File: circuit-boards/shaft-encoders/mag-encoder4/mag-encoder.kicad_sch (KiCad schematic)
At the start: 25 parts, among them J1 CONFIG, J2 0015912055, U1 AP2120N-3.3TRG1, U2 SN74LVC7032ABQAR, U3 MA732GQ

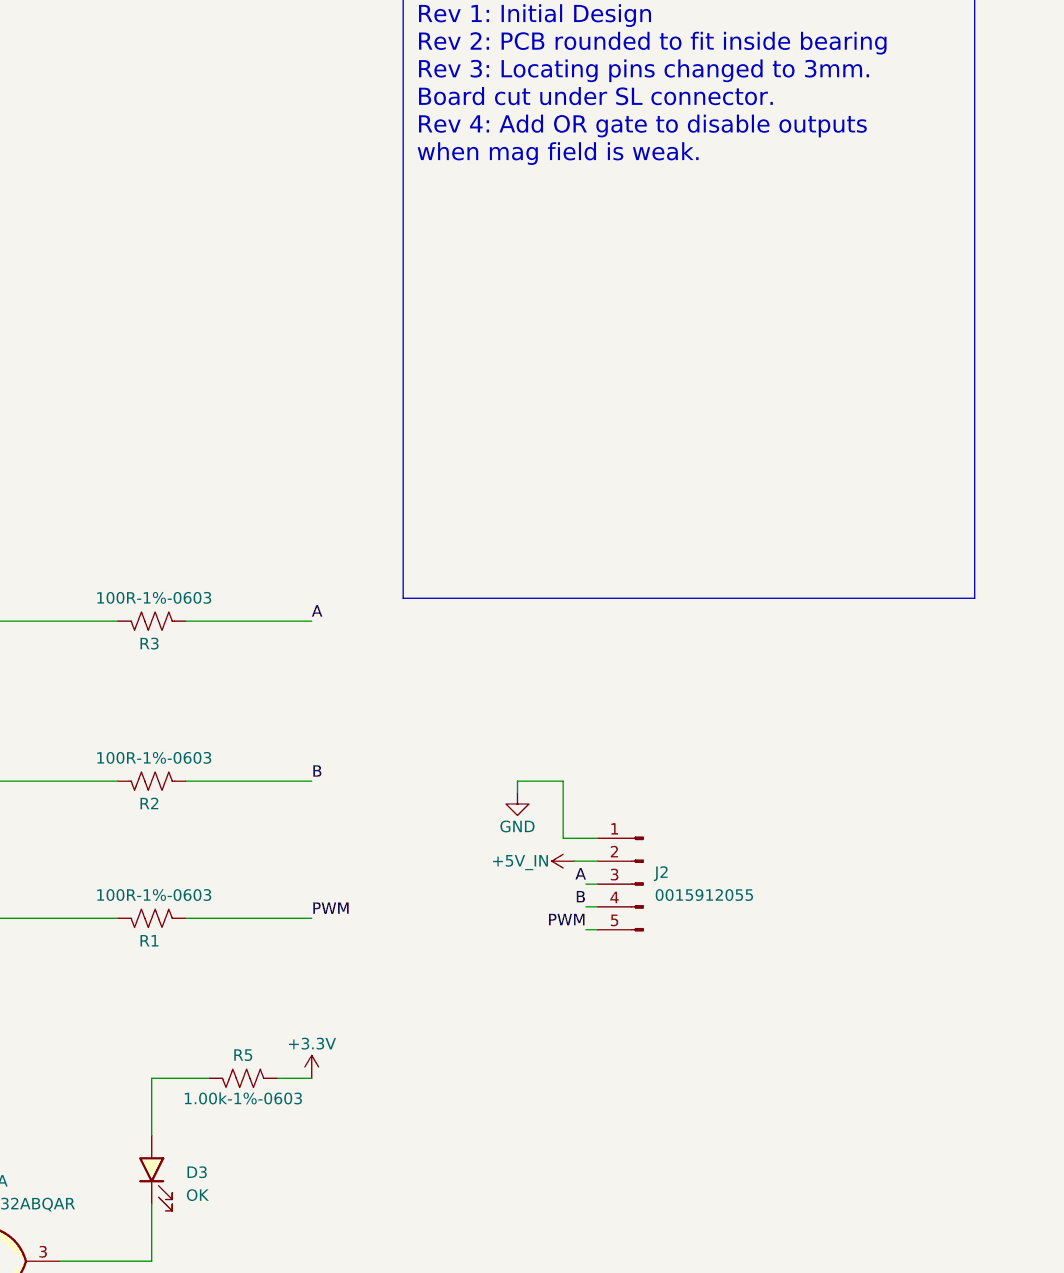
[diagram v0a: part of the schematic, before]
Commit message: Change Green LED current to 5mA
Signed-off-by: scott <sgberman1@gmail.com>
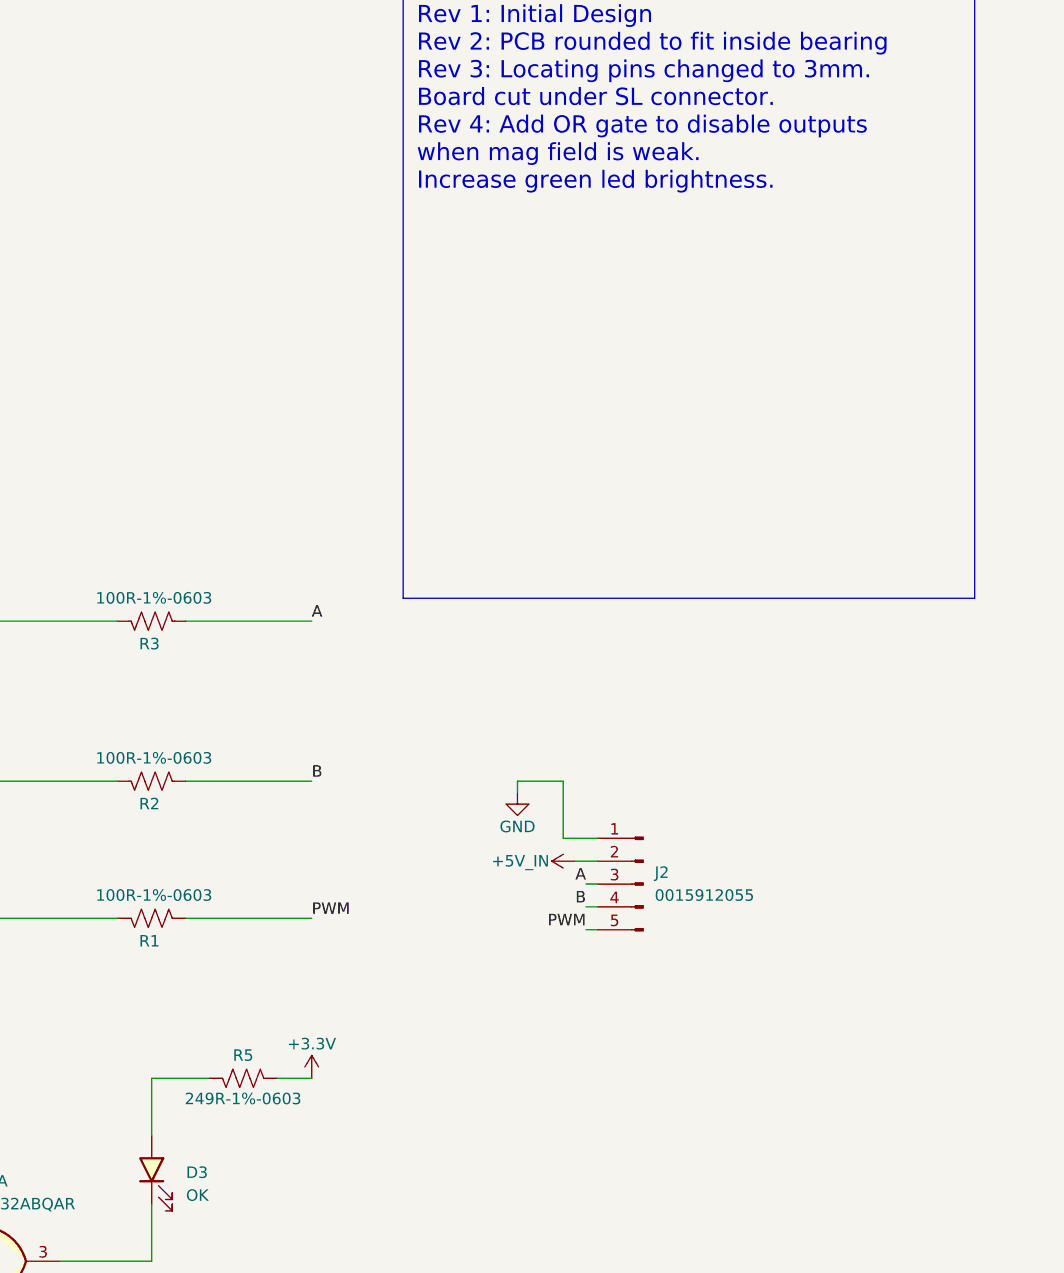
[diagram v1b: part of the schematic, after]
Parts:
- R5: value 1.00k-1%-0603 -> 249R-1%-0603; DIST P/N 311-1.00KHRCT-ND -> 311-249HRCT-ND; MFG P/N RC0603FR-071KL -> RC0603FR-07249RL
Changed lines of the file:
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@@
 	(title_block
 		(title "Mag Encoder")
-		(date "2024-11-25")
+		(date "2024-12-03")
 		(rev "4")
 		(company "971 SPARTAN ROBOTICS")
@@
 		)
 	)
-	(text_box "REVISION NOTES\n=======================\nRev 1: Initial Design\nRev 2: PCB rounded to fit inside bearing\nRev 3: Locating pins changed to 3mm.\n       Board cut under SL connector.\nRev 4: Add OR gate to disable outputs\n       when mag field is weak."
+	(text_box "REVISION NOTES\n=======================\nRev 1: Initial Design\nRev 2: PCB rounded to fit inside bearing\nRev 3: Locating pins changed to 3mm.\n       Board cut under SL connector.\nRev 4: Add OR gate to disable outputs\n       when mag field is weak.\n       Increase green led brightness."
 		(exclude_from_sim no)
 		(at 350.52 17.78 0)
@@
 			)
 		)
-		(property "Value" "1.00k-1%-0603"
+		(property "Value" "249R-1%-0603"
 			(at 332.74 147.066 90)
 			(effects
@@
 			)
 		)
-		(property "DIST P/N" "311-1.00KHRCT-ND"
+		(property "DIST P/N" "311-249HRCT-ND"
 			(at 332.74 144.78 0)
 			(effects
@@
 			)
 		)
-		(property "MFG P/N" "RC0603FR-071KL"
+		(property "MFG P/N" "RC0603FR-07249RL"
 			(at 332.74 144.78 0)
 			(effects

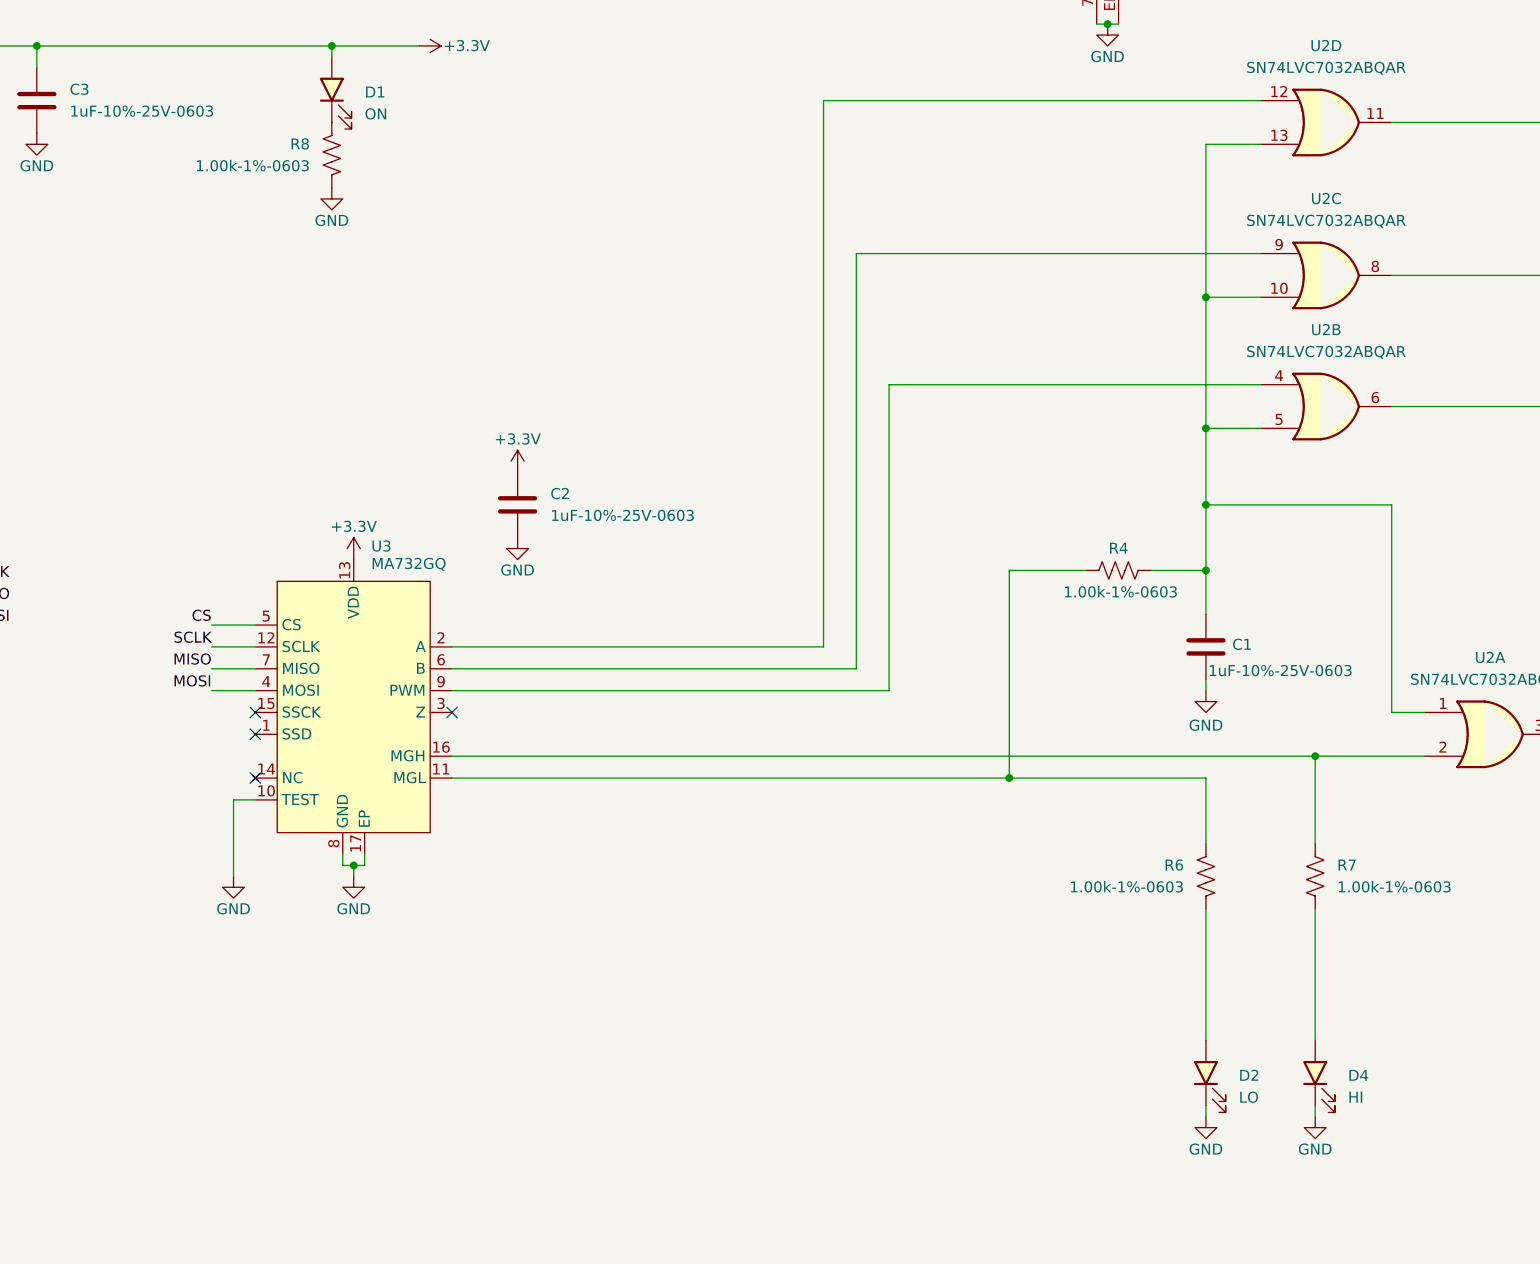
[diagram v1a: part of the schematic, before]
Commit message: Update mag encoder silk and board color
Signed-off-by: scott <sgberman1@gmail.com>
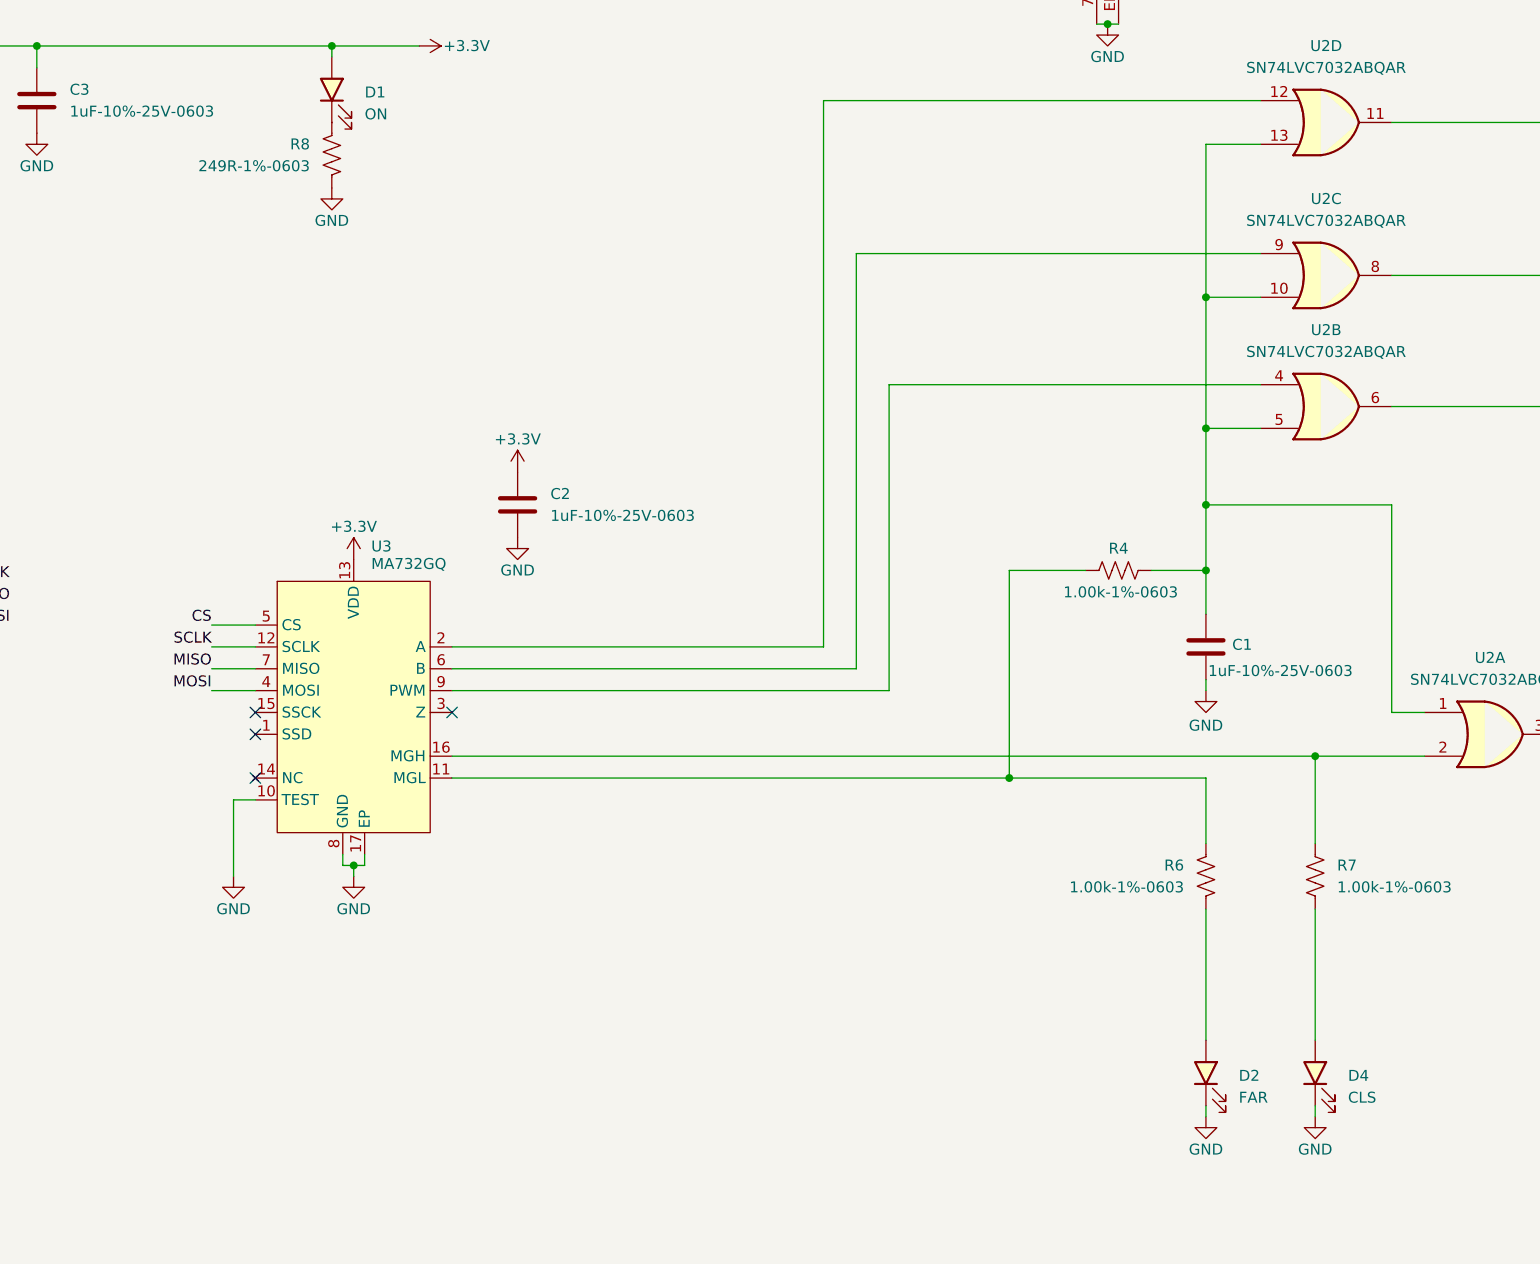
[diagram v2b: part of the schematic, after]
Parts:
- D1: DIST P/N 732-4981-1-ND -> 732-4980-1-ND; MFG P/N 150060YS75000 -> 150060VS75000
- D2: value LO -> FAR
- D4: value HI -> CLS; DIST P/N 732-4978-1-ND -> 732-4981-1-ND; MFG P/N 150060RS75000 -> 150060YS75000
- R8: value 1.00k-1%-0603 -> 249R-1%-0603; DIST P/N 311-1.00KHRCT-ND -> 311-249HRCT-ND; MFG P/N RC0603FR-071KL -> RC0603FR-07249RL
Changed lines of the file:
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@@
 	(title_block
 		(title "Mag Encoder")
-		(date "2024-12-03")
+		(date "2024-12-05")
 		(rev "4")
 		(company "971 SPARTAN ROBOTICS")
@@
 			)
 		)
-		(property "Value" "LO"
+		(property "Value" "FAR"
 			(at 275.59 207.3274 90)
 			(effects
@@
 			)
 		)
-		(property "Value" "HI"
+		(property "Value" "CLS"
 			(at 288.29 207.3274 90)
 			(effects
@@
 			)
 		)
-		(property "DIST P/N" "732-4978-1-ND"
+		(property "DIST P/N" "732-4981-1-ND"
 			(at 284.48 204.47 0)
 			(effects
@@
 			)
 		)
-		(property "MFG P/N" "150060RS75000"
+		(property "MFG P/N" "150060YS75000"
 			(at 284.48 204.47 0)
 			(effects
@@
 			)
 		)
-		(property "Value" "1.00k-1%-0603"
+		(property "Value" "249R-1%-0603"
 			(at 167.64 99.0599 0)
 			(effects
@@
 			)
 		)
-		(property "DIST P/N" "311-1.00KHRCT-ND"
+		(property "DIST P/N" "311-249HRCT-ND"
 			(at 170.18 97.79 0)
 			(effects
@@
 			)
 		)
-		(property "MFG P/N" "RC0603FR-071KL"
+		(property "MFG P/N" "RC0603FR-07249RL"
 			(at 170.18 97.79 0)
 			(effects
@@
 			)
 		)
-		(property "MFG P/N" "150060YS75000"
+		(property "MFG P/N" "150060VS75000"
 			(at 170.18 90.17 0)
 			(effects
@@
 			)
 		)
-		(property "DIST P/N" "732-4981-1-ND"
+		(property "DIST P/N" "732-4980-1-ND"
 			(at 170.18 90.17 0)
 			(effects
